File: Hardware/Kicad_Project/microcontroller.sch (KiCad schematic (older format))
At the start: 40 parts

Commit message: [HARWARE] Add PWM definition around STM32
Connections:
- net UART_AX12_TX: now reaches U?.34 (PA0)
- net UART_AX12_RX: now reaches U?.35 (PA1)
- net PWM1: now reaches U?.4 (PE5)
- net PWM2: now reaches U?.5 (PE6)
- net PWM3: now reaches U?.75 (PB14)
- net PWM4: now reaches U?.76 (PB15)
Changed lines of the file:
@@
-EESchema Schematic File Version 2  date dim. 06 oct. 2013 15:54:58 CEST
+EESchema Schematic File Version 2  date dim. 06 oct. 2013 18:59:37 CEST
 LIBS:power
 LIBS:device
@@
 Comment4 ""
 $EndDescr
+Text HLabel 2950 5400 0    60   Input ~ 0
+UART_AX12_RX
+Text HLabel 2950 5300 0    60   Input ~ 0
+UART_AX12_TX
+Wire Wire Line
+	7500 5300 7550 5300
+Wire Wire Line
+	2950 2300 3000 2300
 Wire Wire Line
 	7550 4600 7500 4600
@@
 Wire Wire Line
 	7550 4700 7500 4700
+Wire Wire Line
+	3000 2400 2950 2400
+Wire Wire Line
+	7550 5200 7500 5200
+Text HLabel 7550 5200 2    60   Input ~ 0
+PWM4
+Text HLabel 7550 5300 2    60   Input ~ 0
+PWM3
+Text HLabel 2950 2400 0    60   Input ~ 0
+PWM2
+Text HLabel 2950 2300 0    60   Input ~ 0
+PWM1
 Text HLabel 7550 4600 2    60   Input ~ 0
 enc4_B

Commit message: [HARWARE] Add AX12 interface
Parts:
- added P?: CONN_4, symbol CONN_4
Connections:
- net GND: now also P?.4 (P4)
- net UART_AX12_RX: now also P?.2 (P2)
- net UART_AX12_TX: now also P?.3 (P3)
- new net AX12_POWER: P?.1 (P1)

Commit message: [HARWARE] Add AX12 power
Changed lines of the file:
@@
-EESchema Schematic File Version 2  date dim. 06 oct. 2013 19:04:08 CEST
+EESchema Schematic File Version 2  date dim. 06 oct. 2013 19:08:01 CEST
 LIBS:power
 LIBS:device
@@
 Comment4 ""
 $EndDescr
+Text Label 9150 3100 2    60   ~ 0
+UART_AX12_RX
+Text Label 9150 3200 2    60   ~ 0
+UART_AX12_TX
+Text Label 2950 5400 2    60   ~ 0
+UART_AX12_RX
+Text Label 2950 5300 2    60   ~ 0
+UART_AX12_TX
 Wire Wire Line
 	9200 3200 9150 3200
@@
 Wire Wire Line
 	9200 3100 9150 3100
-Text HLabel 9150 3200 0    60   Input ~ 0
-UART_AX12_TX
-Text HLabel 9150 3100 0    60   Input ~ 0
-UART_AX12_RX
 Text HLabel 9150 3000 0    60   Input ~ 0
 AX12_POWER
@@
 	1    0    0    -1
 $EndComp
-Text HLabel 2950 5400 0    60   Input ~ 0
-UART_AX12_RX
-Text HLabel 2950 5300 0    60   Input ~ 0
-UART_AX12_TX
 Text HLabel 7550 5200 2    60   Input ~ 0
 PWM4

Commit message: [HARDWARE] Add MOSI, MISO and SCK to SD card interface
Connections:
- net MISO_SD: now reaches U?.28 (PC2)
- net MOSI_SD: now reaches U?.29 (PC3)
- net SCK_SD: now reaches U?.74 (PB13)

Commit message: [HARDWARE] Add SPI interface
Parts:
- added P?: CONN_4, symbol CONN_4
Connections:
- net GND: now also P?.4 (P4)
- net PC11: now also P?.2 (P2)
- net SPI_SCK: now reaches U?.111 (PC10)
- net SPI_SCK: now also P?.3 (P3)
- net SPI_MOSI: now reaches U?.113 (PC12)
- net SPI_MOSI: now also P?.1 (P1)

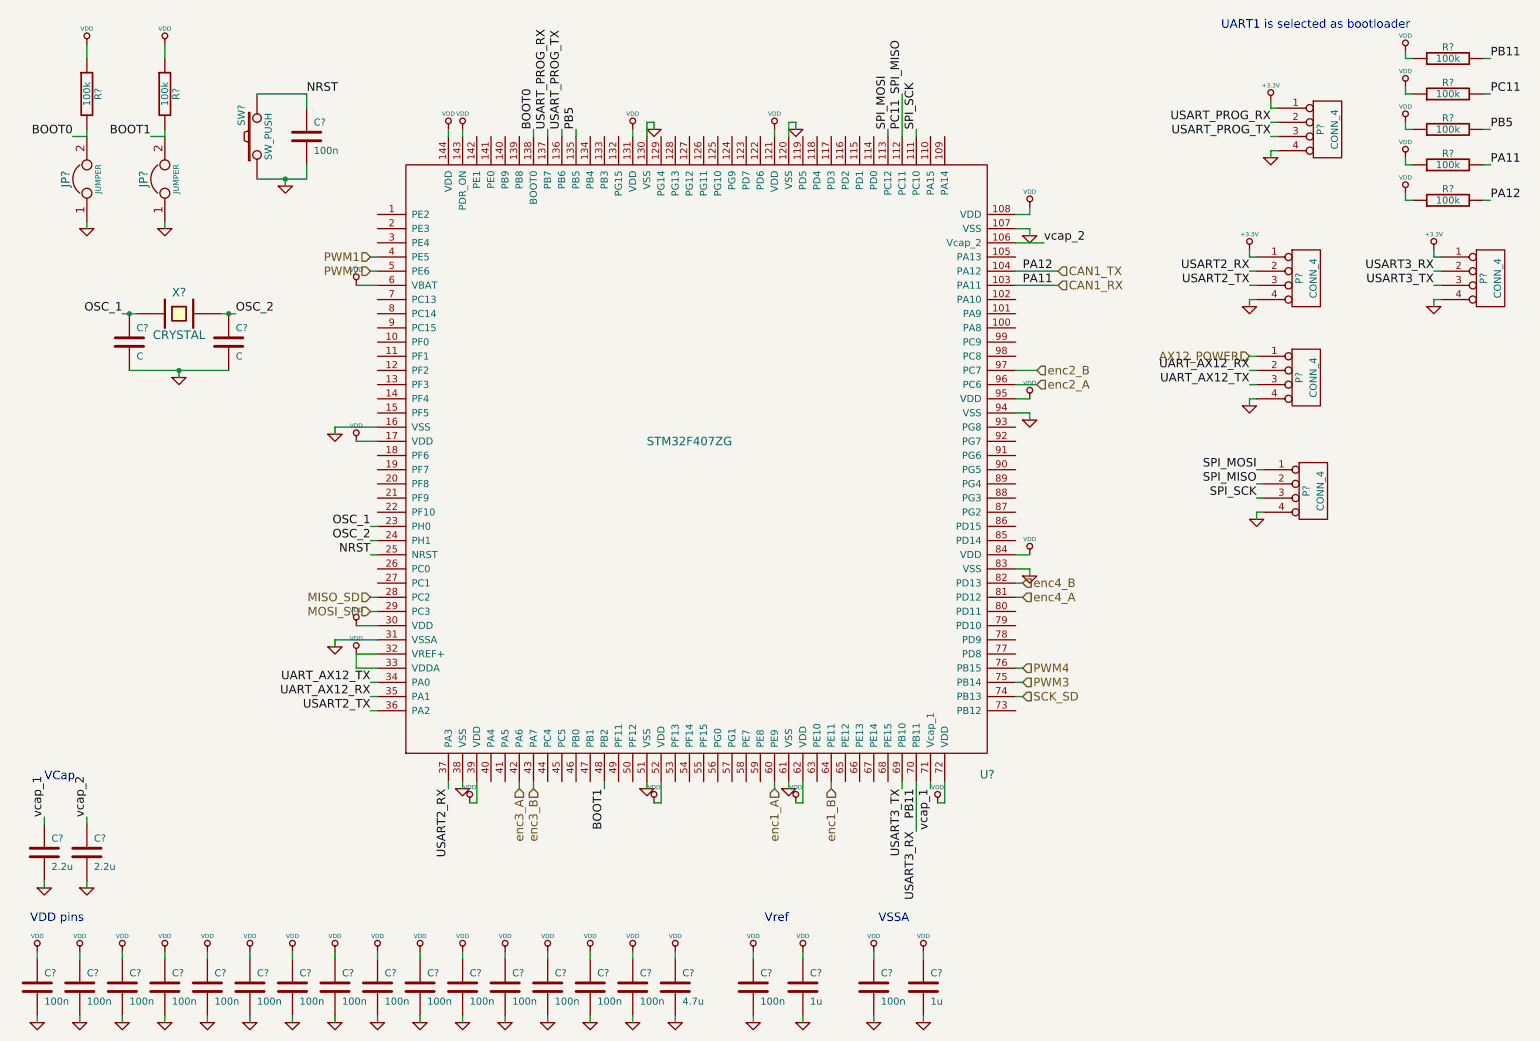
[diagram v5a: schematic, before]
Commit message: [HARDWARE] Add I2C interface
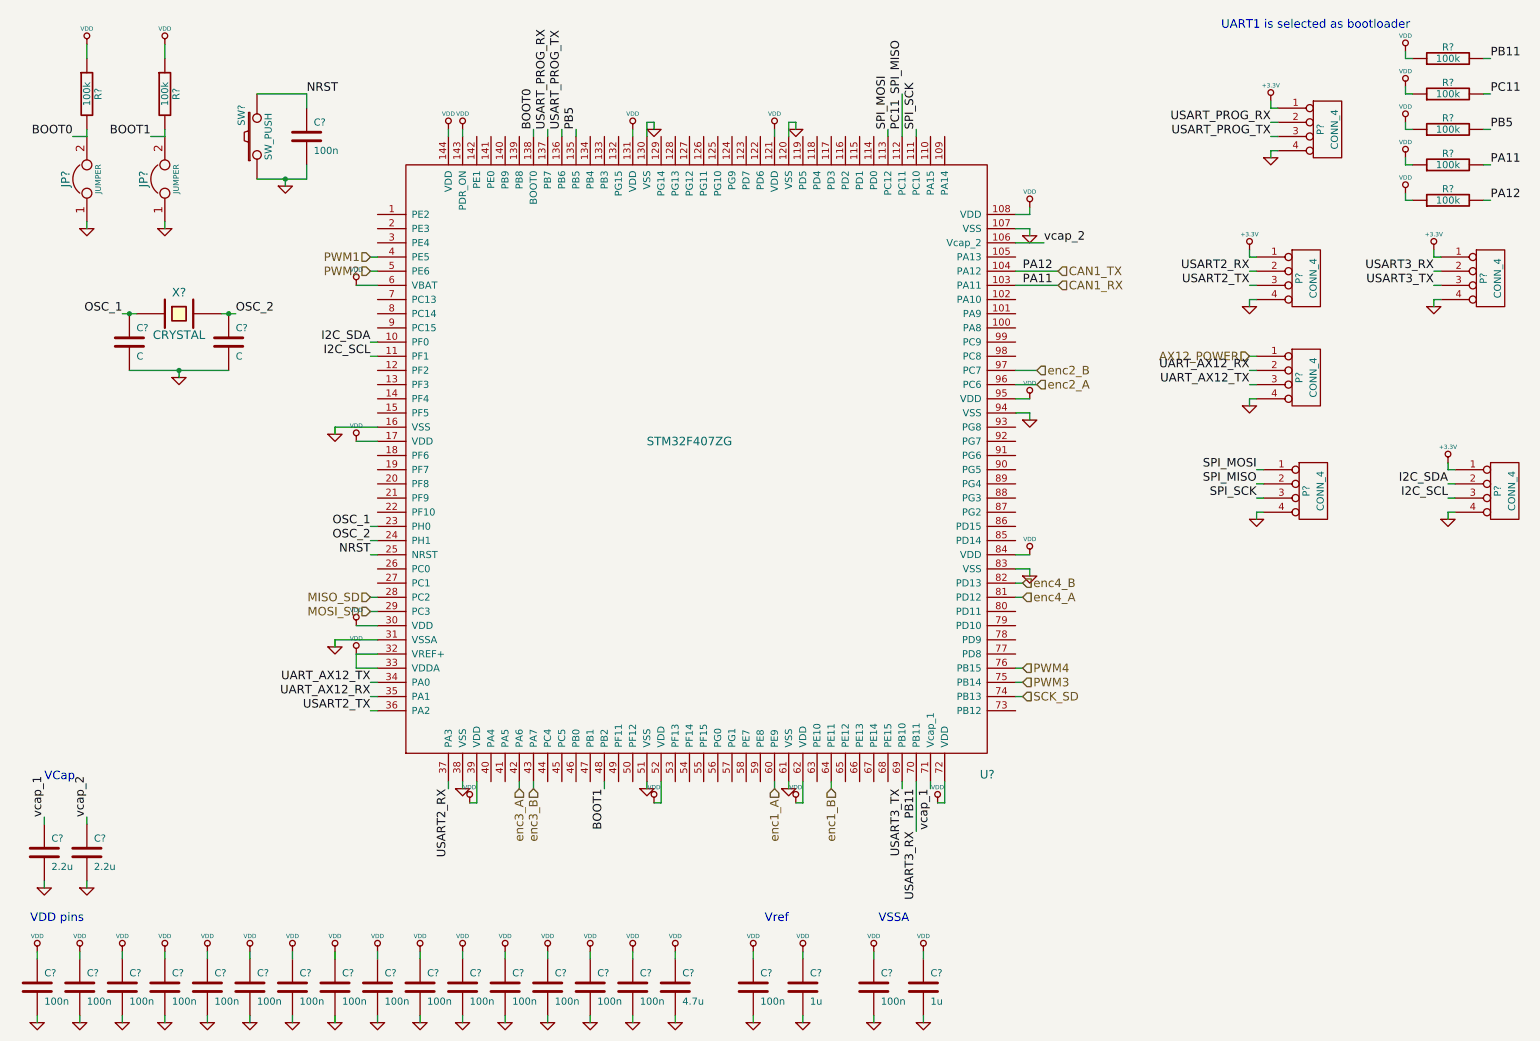
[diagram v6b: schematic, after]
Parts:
- added P?: CONN_4, symbol CONN_4
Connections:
- net +3.3V: now also P?.1 (P1)
- net GND: now also P?.4 (P4)
- net I2C_SDA: now reaches U?.10 (PF0)
- net I2C_SDA: now also P?.2 (P2)
- net I2C_SCL: now reaches U?.11 (PF1)
- net I2C_SCL: now also P?.3 (P3)

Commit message: [HARDWARE] Add 4 servo interface
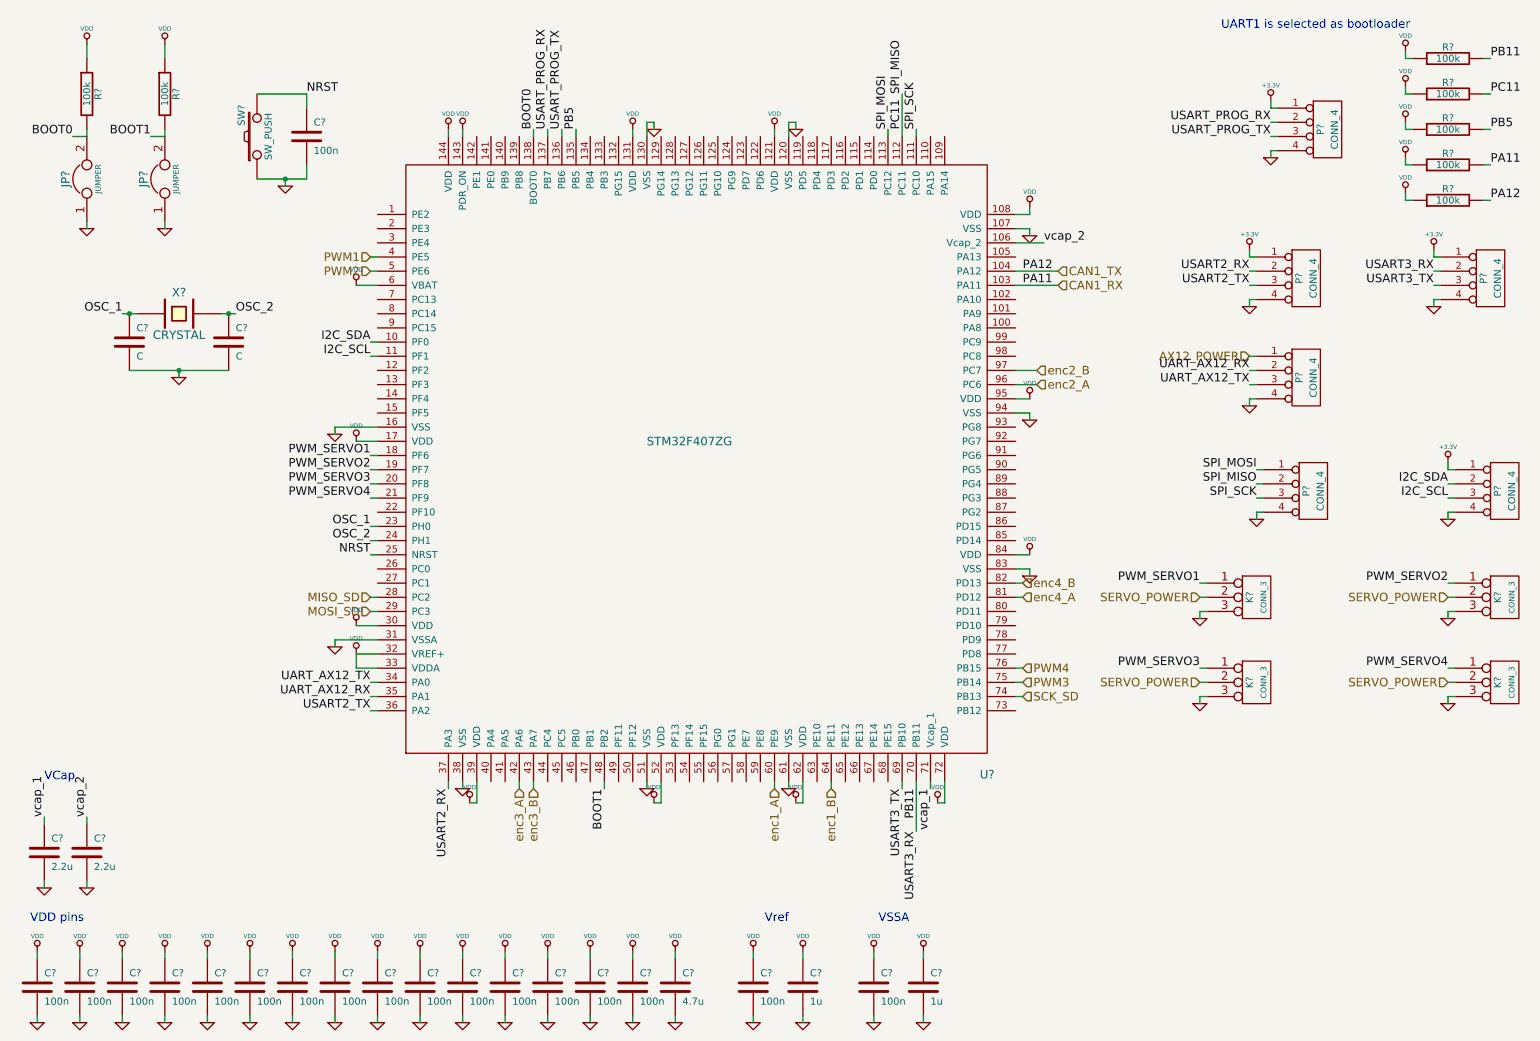
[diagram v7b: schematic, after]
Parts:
- added K? (x4): CONN_3, symbol CONN_3
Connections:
- net GND: now also K?.3 (P3), K?.3 (P3), K?.3 (P3), K?.3 (P3)
- net PWM_SERVO1: now reaches U?.18 (PF6)
- net PWM_SERVO1: now also K?.1 (P1)
- net PWM_SERVO2: now reaches U?.19 (PF7)
- net PWM_SERVO2: now also K?.1 (P1)
- net PWM_SERVO3: now reaches U?.20 (PF8)
- net PWM_SERVO3: now also K?.1 (P1)
- net PWM_SERVO4: now reaches U?.21 (PF9)
- net PWM_SERVO4: now also K?.1 (P1)
- new net SERVO_POWER: K?.2 (PM), K?.2 (PM), K?.2 (PM), K?.2 (PM)

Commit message: [HARDWARE] Add ADC and GP2 interfaces
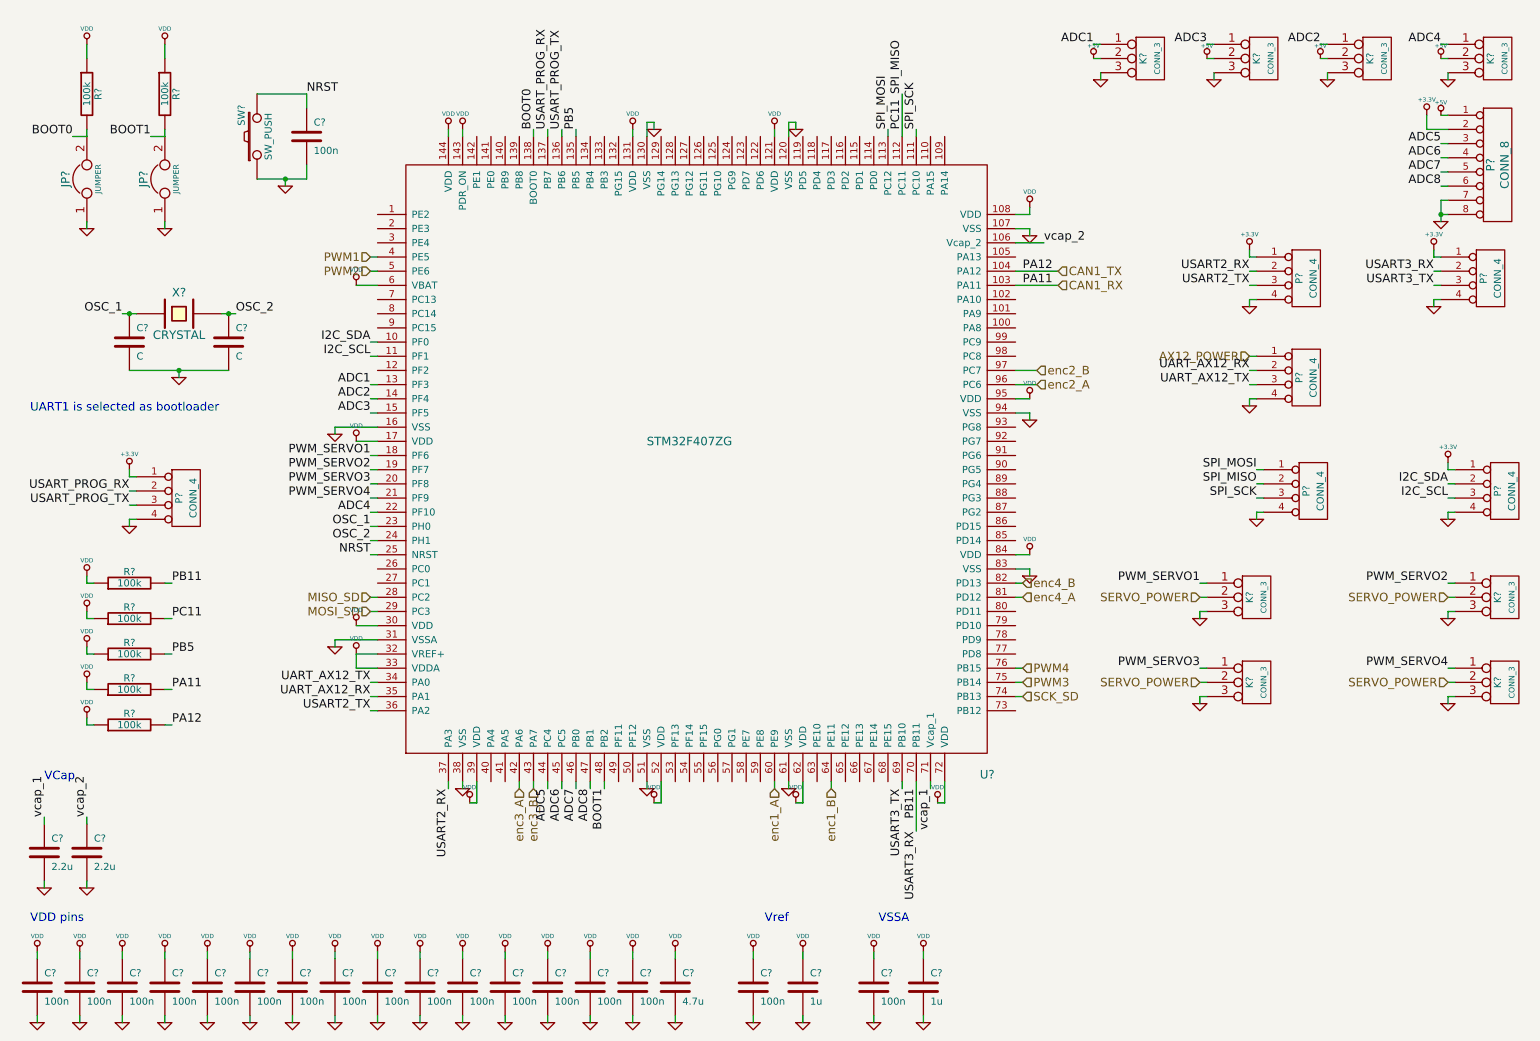
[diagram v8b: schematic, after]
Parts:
- added K? (x4): CONN_3, symbol CONN_3
- added P?: CONN_8, symbol CONN_8
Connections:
- net +3.3V: now also P?.2 (P2)
- net GND: now also K?.3 (P3), K?.3 (P3), K?.3 (P3), K?.3 (P3), P?.7 (P7), P?.8 (P8)
- net ADC1: now reaches U?.13 (PF3)
- net ADC1: now also K?.1 (P1)
- net ADC2: now reaches U?.14 (PF4)
- net ADC2: now also K?.1 (P1)
- net ADC3: now reaches U?.15 (PF5)
- net ADC3: now also K?.1 (P1)
- net ADC4: now reaches U?.22 (PF10)
- net ADC4: now also K?.1 (P1)
- net ADC5: now reaches U?.44 (PC4)
- net ADC5: now also P?.3 (P3)
- net ADC6: now reaches U?.45 (PC5)
- net ADC6: now also P?.4 (P4)
- net ADC7: now reaches U?.46 (PB0)
- net ADC7: now also P?.5 (P5)
- net ADC8: now reaches U?.47 (PB1)
- net ADC8: now also P?.6 (P6)
- new net +5V: K?.2 (PM), K?.2 (PM), K?.2 (PM), K?.2 (PM), P?.1 (P1)
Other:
- moved on the sheet: P?, R?
